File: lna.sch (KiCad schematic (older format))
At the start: 21 parts, among them P1 CONN_1, P2 CONN_2, P3 CONN_1, P4 CONN_1, Q1 BFG540W, U1 LM7810CT

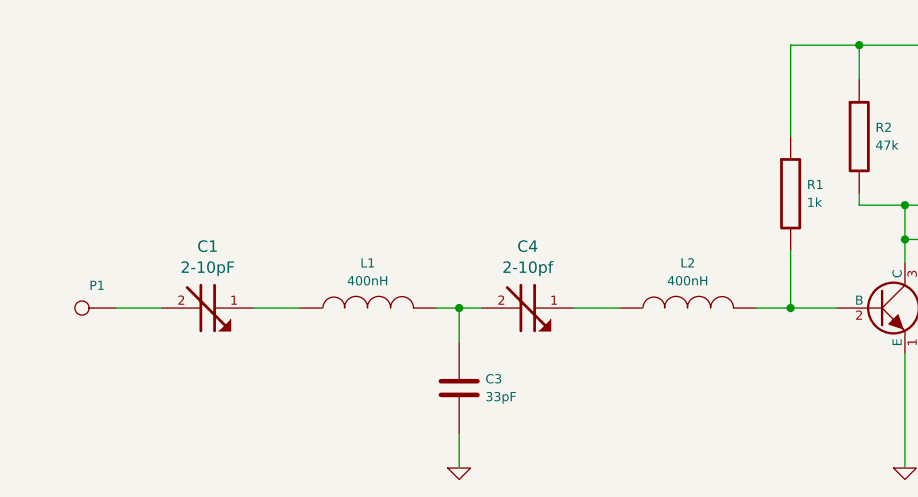
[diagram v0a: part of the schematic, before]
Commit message: Those are called LC filters not CL filters ... D'oh
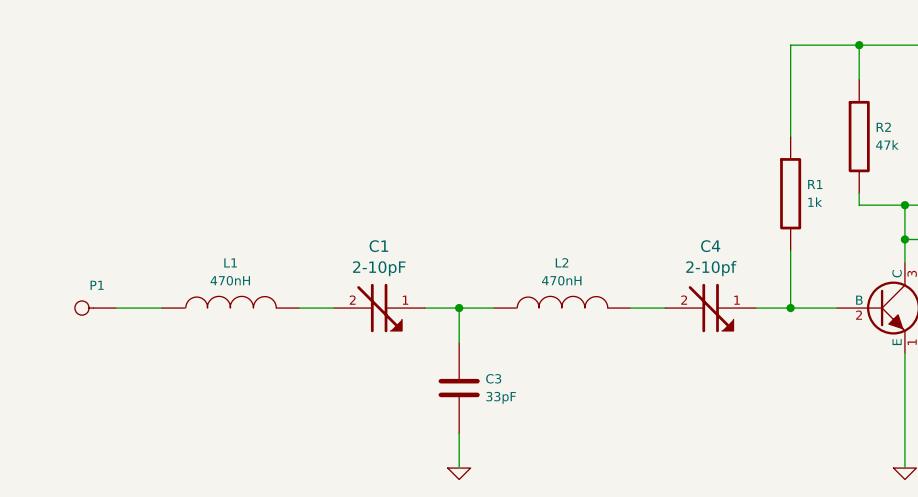
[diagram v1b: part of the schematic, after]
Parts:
- L1, L2: value 400nH -> 470nH
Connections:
- net at P1.1: now also L1.1; no longer C1.2
- net at C1.1: now also C3.1, L2.1; no longer L1.1
- net at C4.1: now also Q1.2 (B), R1.2; no longer L2.1
- new net: C1.2, L1.2
- new net: C4.2, L2.2
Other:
- moved on the sheet: C1, C4, L1, L2
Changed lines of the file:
@@
 L INDUCTOR L1
 U 1 1 56AD3311
-P 4500 4750
-F 0 "L1" V 4696 4750 40  0000 C CNN
-F 1 "400nH" V 4618 4750 40  0000 C CNN
-F 2 "SM1008:SM1008" H 4500 4750 60  0001 C CNN
-F 3 "" H 4500 4750 60  0000 C CNN
-	1    4500 4750
+P 3900 4750
+F 0 "L1" V 4096 4750 40  0000 C CNN
+F 1 "470nH" V 4018 4750 40  0000 C CNN
+F 2 "SM1008:SM1008" H 3900 4750 60  0001 C CNN
+F 3 "" H 3900 4750 60  0000 C CNN
+	1    3900 4750
 	0    -1   -1   0
 $EndComp
@@
 L CTRIM C1
 U 1 1 56AD345C
-P 3800 4750
-F 0 "C1" V 3531 4750 50  0000 C CNN
-F 1 "2-10pF" V 3623 4750 50  0000 C CNN
-F 2 "tzc3:TZC3" H 3800 4750 60  0001 C CNN
-F 3 "" H 3800 4750 60  0000 C CNN
-	1    3800 4750
+P 4550 4750
+F 0 "C1" V 4281 4750 50  0000 C CNN
+F 1 "2-10pF" V 4373 4750 50  0000 C CNN
+F 2 "tzc3:TZC3" H 4550 4750 60  0001 C CNN
+F 3 "" H 4550 4750 60  0000 C CNN
+	1    4550 4750
 	0    1    1    0
 $EndComp
 Wire Wire Line
 	3400 4750 3600 4750
-Wire Wire Line
-	4000 4750 4200 4750
 $Comp
 L C C3
@@
 L INDUCTOR L2
 U 1 1 56AD3814
-P 5900 4750
-F 0 "L2" V 6096 4750 40  0000 C CNN
-F 1 "400nH" V 6018 4750 40  0000 C CNN
-F 2 "SM1008:SM1008" H 5900 4750 60  0001 C CNN
-F 3 "" H 5900 4750 60  0000 C CNN
-	1    5900 4750
+P 5350 4750
+F 0 "L2" V 5546 4750 40  0000 C CNN
+F 1 "470nH" V 5468 4750 40  0000 C CNN
+F 2 "SM1008:SM1008" H 5350 4750 60  0001 C CNN
+F 3 "" H 5350 4750 60  0000 C CNN
+	1    5350 4750
 	0    -1   -1   0
 $EndComp
@@
 L CTRIM C4
 U 1 1 56AD381A
-P 5200 4750
-F 0 "C4" V 4931 4750 50  0000 C CNN
-F 1 "2-10pf" V 5023 4750 50  0000 C CNN
-F 2 "tzc3:TZC3" H 5200 4750 60  0001 C CNN
-F 3 "" H 5200 4750 60  0000 C CNN
-	1    5200 4750
+P 6000 4750
+F 0 "C4" V 5731 4750 50  0000 C CNN
+F 1 "2-10pf" V 5823 4750 50  0000 C CNN
+F 2 "tzc3:TZC3" H 6000 4750 60  0001 C CNN
+F 3 "" H 6000 4750 60  0000 C CNN
+	1    6000 4750
 	0    1    1    0
 $EndComp
 Wire Wire Line
-	4800 4750 5000 4750
-Wire Wire Line
-	5400 4750 5600 4750
+	4750 4750 5050 4750
 Wire Wire Line
 	4900 4900 4900 4750
@@
 Text Notes 2850 2200 0    60   ~ 0
 Shield
+Wire Wire Line
+	4200 4750 4350 4750
+Wire Wire Line
+	5650 4750 5800 4750
 $EndSCHEMATC
